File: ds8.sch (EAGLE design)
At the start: 79 parts, among them Q1 BC850, Q2 BC850, Q3 BC850, U1 LM13700M, U2 LM324, U3 LM324, U4 LM741D

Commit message: added some text infos
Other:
- note added: "Controls"
- note added: "Envelope"
- note added: "LFO"
- note added: "Noise"
- note added: "Output"
- note added: "Power Supply"
- note added: "VCA"
- note added: "VCO"
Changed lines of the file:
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@@
 <?xml version="1.0" encoding="utf-8"?>
 <!DOCTYPE eagle SYSTEM "eagle.dtd">
-<eagle version="6.1">
+<eagle version="6.3">
 <drawing>
 <settings>
@@
 <sheet>
 <plain>
+<text x="-25.4" y="-63.5" size="5.08" layer="91">Power Supply</text>
+<text x="7.62" y="48.26" size="5.08" layer="91">Envelope</text>
+<text x="167.64" y="30.48" size="5.08" layer="91">VCA</text>
+<text x="254" y="5.08" size="5.08" layer="91">Output</text>
+<text x="157.48" y="-111.76" size="5.08" layer="91">Noise</text>
+<text x="149.86" y="-40.64" size="5.08" layer="91">VCO</text>
+<text x="22.86" y="-25.4" size="5.08" layer="91">LFO</text>
+<text x="2.54" y="-121.92" size="5.08" layer="91">Controls</text>
 </plain>
 <instances>

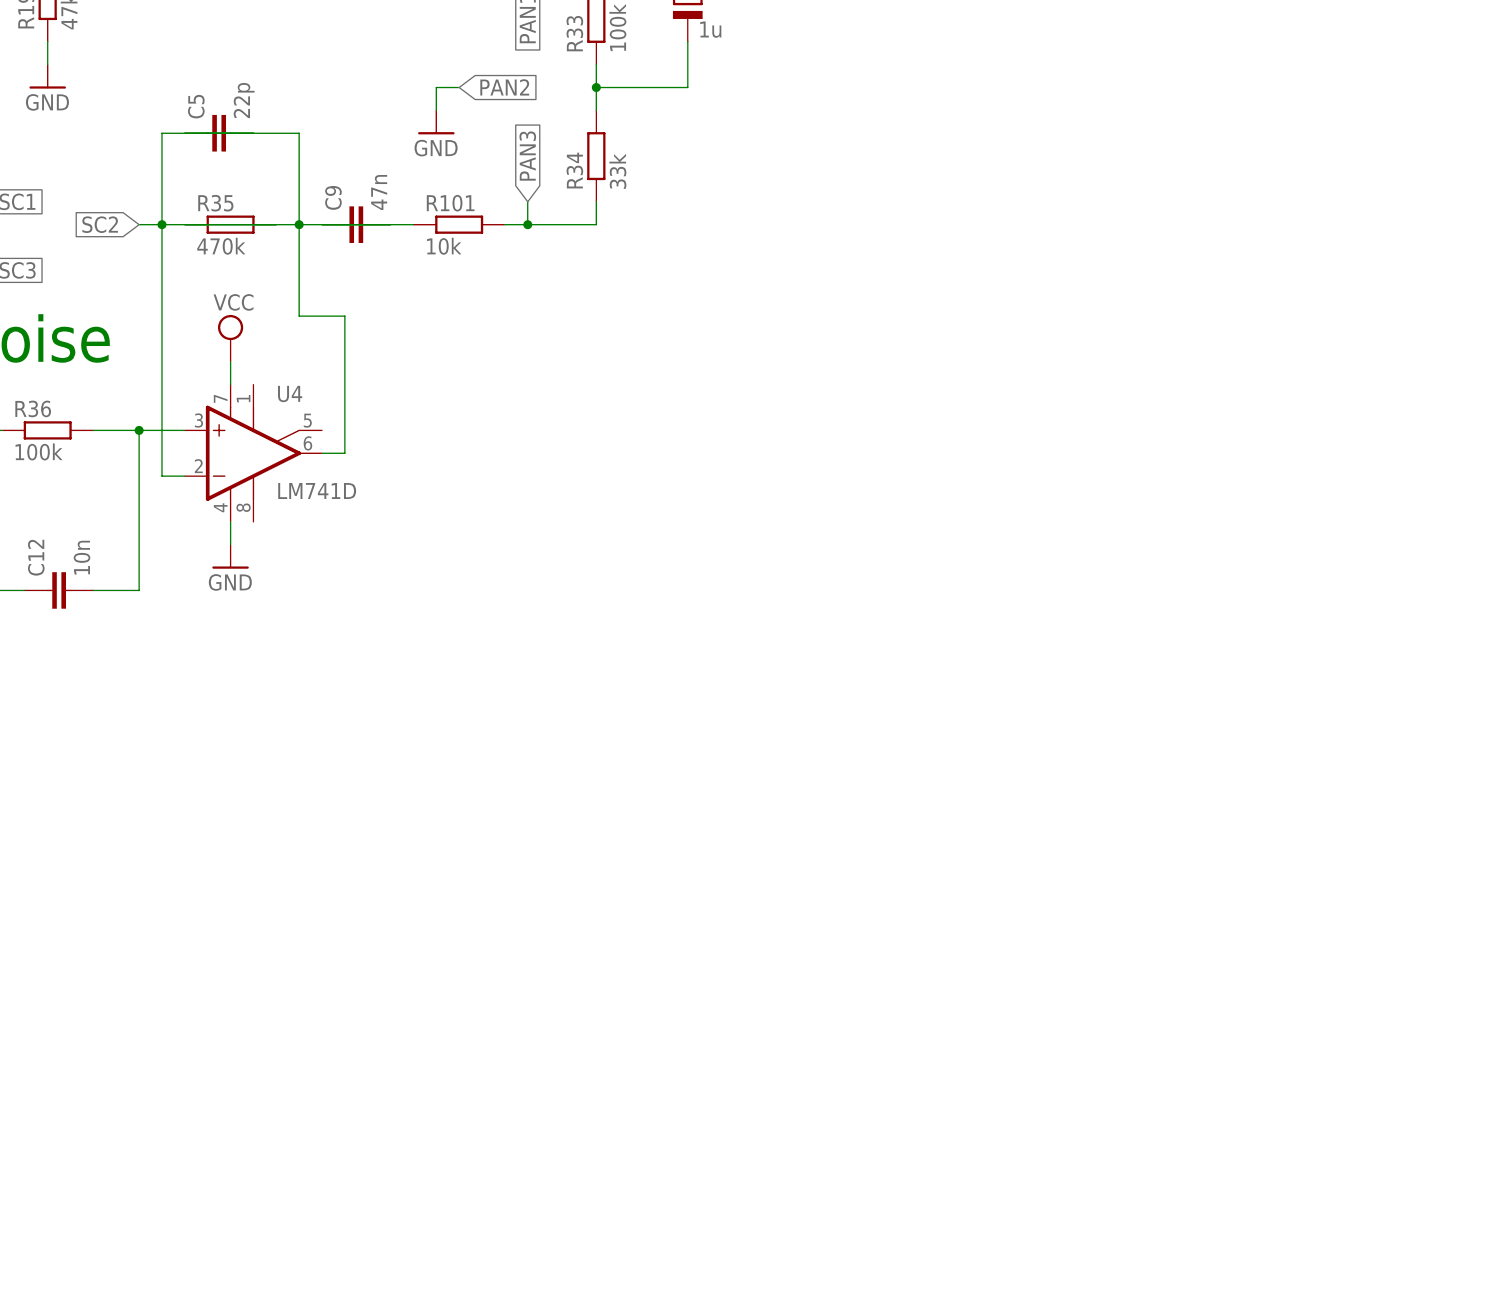
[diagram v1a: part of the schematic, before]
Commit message: added regulator for mcu
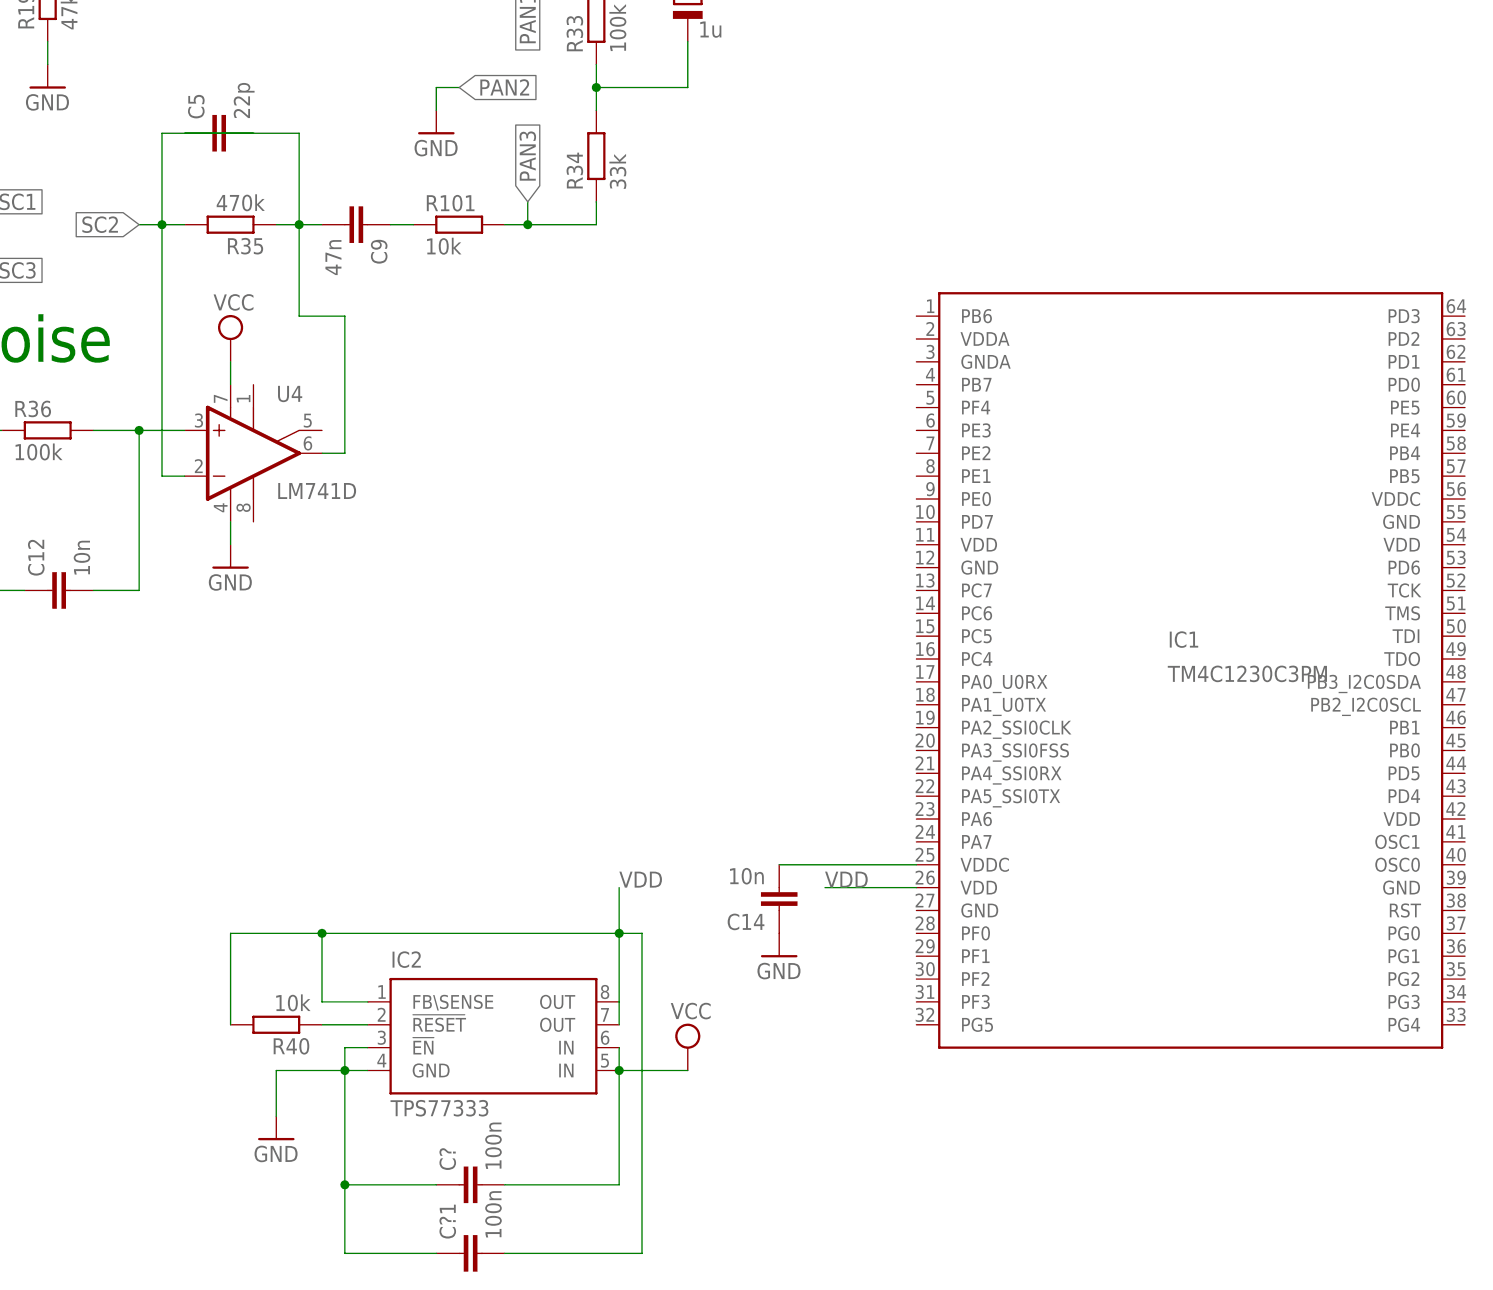
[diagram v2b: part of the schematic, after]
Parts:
- added C14: 10n, rcl:C-EUC1206
- added C?, C?1: 100n, rcl:C-EUC1206
- added IC1: TM4C1230C3PM, TM4:TM4C1230C3PM
- added IC2: TPS77333, texas:TPS77333
- added R40: 10k, rcl:R-EU_M0805
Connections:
- new net N$18: IC2.!RESET, R40.1
- new net N$6: C14.2, IC1.VDDC@0
- new net VDD: C?1.2, IC1.VDD@1, IC2.FB\SENSE, IC2.OUT@1, IC2.OUT@2, R40.2
- net GND: now also C14.1, C?.1, C?1.1, IC2.!EN, IC2.GND
- net VCC: now also C?.2, IC2.IN@1, IC2.IN@2
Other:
- moved on the sheet: C9, R35
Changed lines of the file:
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@@
 <part name="GND30" library="supply1" deviceset="GND" device=""/>
 <part name="GND31" library="supply1" deviceset="GND" device=""/>
+<part name="IC1" library="TM4" deviceset="TM4C1230C3PM" device=""/>
+<part name="IC2" library="texas" deviceset="TPS773*" device="" technology="33"/>
+<part name="SUPPLY10" library="supply2" deviceset="VCC" device=""/>
+<part name="GND32" library="supply1" deviceset="GND" device=""/>
+<part name="C?" library="rcl" deviceset="C-EU" device="C1206" value="100n"/>
+<part name="C?1" library="rcl" deviceset="C-EU" device="C1206" value="100n"/>
+<part name="R40" library="rcl" deviceset="R-EU_" device="M0805" value="10k"/>
+<part name="C14" library="rcl" deviceset="C-EU" device="C1206" value="10n"/>
+<part name="GND33" library="supply1" deviceset="GND" device=""/>
 </parts>
 <sheets>
@@
 <instance part="R33" gate="G$1" x="228.6" y="-73.66" rot="R90"/>
 <instance part="R34" gate="G$1" x="228.6" y="-88.9" rot="R90"/>
-<instance part="R35" gate="G$1" x="187.96" y="-96.52"/>
+<instance part="R35" gate="G$1" x="187.96" y="-96.52" rot="R180"/>
 <instance part="R36" gate="G$1" x="167.64" y="-119.38"/>
 <instance part="R37" gate="G$1" x="144.78" y="-129.54"/>
@@
 <instance part="SUPPLY6" gate="G$1" x="137.16" y="27.94"/>
 <instance part="GND15" gate="1" x="213.36" y="-43.18"/>
-<instance part="C9" gate="G$1" x="200.66" y="-96.52" rot="R90"/>
+<instance part="C9" gate="G$1" x="203.2" y="-96.52" rot="R270"/>
 <instance part="C10" gate="G$1" x="152.4" y="-93.98" rot="R90"/>
 <instance part="C11" gate="G$1" x="152.4" y="-101.6" rot="R90"/>
@@
 <instance part="GND30" gate="1" x="40.64" y="-172.72"/>
 <instance part="GND31" gate="1" x="68.58" y="-172.72"/>
+<instance part="IC1" gate="G$1" x="294.64" y="-144.78"/>
+<instance part="IC2" gate="G$1" x="215.9" y="-187.96"/>
+<instance part="SUPPLY10" gate="G$1" x="238.76" y="-187.96"/>
+<instance part="GND32" gate="1" x="193.04" y="-198.12"/>
+<instance part="C?" gate="G$1" x="213.36" y="-203.2" rot="R90"/>
+<instance part="C?1" gate="G$1" x="213.36" y="-210.82" rot="R90"/>
+<instance part="R40" gate="G$1" x="193.04" y="-185.42" rot="R180"/>
+<instance part="C14" gate="G$1" x="248.92" y="-172.72" rot="R180"/>
+<instance part="GND33" gate="1" x="248.92" y="-177.8"/>
 </instances>
 <busses>
@@
 <pinref part="GND29" gate="1" pin="GND"/>
 </segment>
+<segment>
+<pinref part="IC2" gate="G$1" pin="GND"/>
+<wire x1="203.2" y1="-190.5" x2="200.66" y2="-190.5" width="0.1524" layer="91"/>
+<pinref part="GND32" gate="1" pin="GND"/>
+<wire x1="200.66" y1="-190.5" x2="193.04" y2="-190.5" width="0.1524" layer="91"/>
+<wire x1="193.04" y1="-190.5" x2="193.04" y2="-195.58" width="0.1524" layer="91"/>
+<pinref part="IC2" gate="G$1" pin="!EN"/>
+<wire x1="203.2" y1="-187.96" x2="200.66" y2="-187.96" width="0.1524" layer="91"/>
+<wire x1="200.66" y1="-187.96" x2="200.66" y2="-190.5" width="0.1524" layer="91"/>
+<junction x="200.66" y="-190.5"/>
+<pinref part="C?" gate="G$1" pin="1"/>
+<wire x1="210.82" y1="-203.2" x2="200.66" y2="-203.2" width="0.1524" layer="91"/>
+<wire x1="200.66" y1="-203.2" x2="200.66" y2="-190.5" width="0.1524" layer="91"/>
+<wire x1="200.66" y1="-203.2" x2="200.66" y2="-210.82" width="0.1524" layer="91"/>
+<pinref part="C?1" gate="G$1" pin="1"/>
+<wire x1="200.66" y1="-210.82" x2="210.82" y2="-210.82" width="0.1524" layer="91"/>
+<junction x="200.66" y="-203.2"/>
+</segment>
+<segment>
+<pinref part="C14" gate="G$1" pin="1"/>
+<pinref part="GND33" gate="1" pin="GND"/>
+</segment>
 </net>
 <net name="VCC" class="0">
@@
 <wire x1="121.92" y1="-127" x2="121.92" y2="-129.54" width="0.1524" layer="91"/>
 <junction x="121.92" y="-129.54"/>
+</segment>
+<segment>
+<pinref part="IC2" gate="G$1" pin="IN@1"/>
+<pinref part="IC2" gate="G$1" pin="IN@2"/>
+<wire x1="231.14" y1="-190.5" x2="231.14" y2="-187.96" width="0.1524" layer="91"/>
+<pinref part="SUPPLY10" gate="G$1" pin="VCC"/>
+<wire x1="238.76" y1="-190.5" x2="231.14" y2="-190.5" width="0.1524" layer="91"/>
+<wire x1="231.14" y1="-190.5" x2="231.14" y2="-203.2" width="0.1524" layer="91"/>
+<pinref part="C?" gate="G$1" pin="2"/>
+<wire x1="231.14" y1="-203.2" x2="218.44" y2="-203.2" width="0.1524" layer="91"/>
+<junction x="231.14" y="-190.5"/>
 </segment>
 </net>
@@
 <pinref part="R101" gate="G$1" pin="1"/>
 <pinref part="C9" gate="G$1" pin="1"/>
-<wire x1="208.28" y1="-96.52" x2="198.12" y2="-96.52" width="0.1524" layer="91"/>
+<wire x1="208.28" y1="-96.52" x2="205.74" y2="-96.52" width="0.1524" layer="91"/>
 </segment>
 </net>
@@
 <pinref part="C9" gate="G$1" pin="2"/>
 <pinref part="R35" gate="G$1" pin="1"/>
-<wire x1="205.74" y1="-96.52" x2="195.58" y2="-96.52" width="0.1524" layer="91"/>
+<wire x1="198.12" y1="-96.52" x2="195.58" y2="-96.52" width="0.1524" layer="91"/>
 <pinref part="C5" gate="G$1" pin="1"/>
-<wire x1="195.58" y1="-96.52" x2="182.88" y2="-96.52" width="0.1524" layer="91"/>
+<wire x1="195.58" y1="-96.52" x2="193.04" y2="-96.52" width="0.1524" layer="91"/>
 <wire x1="182.88" y1="-86.36" x2="195.58" y2="-86.36" width="0.1524" layer="91"/>
 <wire x1="195.58" y1="-86.36" x2="195.58" y2="-96.52" width="0.1524" layer="91"/>
@@
 <segment>
 <pinref part="R35" gate="G$1" pin="2"/>
-<wire x1="193.04" y1="-96.52" x2="180.34" y2="-96.52" width="0.1524" layer="91"/>
+<wire x1="182.88" y1="-96.52" x2="180.34" y2="-96.52" width="0.1524" layer="91"/>
 <wire x1="180.34" y1="-96.52" x2="180.34" y2="-86.36" width="0.1524" layer="91"/>
 <pinref part="C5" gate="G$1" pin="2"/>
@@
 </segment>
 </net>
+<net name="VDD" class="0">
+<segment>
+<pinref part="IC2" gate="G$1" pin="OUT@1"/>
+<pinref part="IC2" gate="G$1" pin="OUT@2"/>
+<wire x1="231.14" y1="-185.42" x2="231.14" y2="-182.88" width="0.1524" layer="91"/>
+<wire x1="231.14" y1="-182.88" x2="231.14" y2="-175.26" width="0.1524" layer="91"/>
+<label x="231.14" y="-170.18" size="1.778" layer="95"/>
+<pinref part="IC2" gate="G$1" pin="FB\SENSE"/>
+<wire x1="231.14" y1="-175.26" x2="231.14" y2="-170.18" width="0.1524" layer="91"/>
+<wire x1="203.2" y1="-182.88" x2="198.12" y2="-182.88" width="0.1524" layer="91"/>
+<wire x1="198.12" y1="-182.88" x2="198.12" y2="-175.26" width="0.1524" layer="91"/>
+<wire x1="198.12" y1="-175.26" x2="231.14" y2="-175.26" width="0.1524" layer="91"/>
+<junction x="231.14" y="-175.26"/>
+<pinref part="C?1" gate="G$1" pin="2"/>
+<wire x1="218.44" y1="-210.82" x2="233.68" y2="-210.82" width="0.1524" layer="91"/>
+<wire x1="233.68" y1="-210.82" x2="233.68" y2="-175.26" width="0.1524" layer="91"/>
+<wire x1="233.68" y1="-175.26" x2="231.14" y2="-175.26" width="0.1524" layer="91"/>
+<pinref part="R40" gate="G$1" pin="2"/>
+<wire x1="187.96" y1="-185.42" x2="187.96" y2="-175.26" width="0.1524" layer="91"/>
+<wire x1="187.96" y1="-175.26" x2="198.12" y2="-175.26" width="0.1524" layer="91"/>
+<junction x="198.12" y="-175.26"/>
+</segment>
+<segment>
+<pinref part="IC1" gate="G$1" pin="VDD@1"/>
+<label x="254" y="-170.18" size="1.778" layer="95"/>
+<wire x1="254" y1="-170.18" x2="264.16" y2="-170.18" width="0.1524" layer="91"/>
+</segment>
+</net>
+<net name="N$18" class="0">
+<segment>
+<pinref part="IC2" gate="G$1" pin="!RESET"/>
+<pinref part="R40" gate="G$1" pin="1"/>
+<wire x1="203.2" y1="-185.42" x2="198.12" y2="-185.42" width="0.1524" layer="91"/>
+</segment>
+</net>
+<net name="N$6" class="0">
+<segment>
+<pinref part="IC1" gate="G$1" pin="VDDC@0"/>
+<pinref part="C14" gate="G$1" pin="2"/>
+<wire x1="264.16" y1="-167.64" x2="248.92" y2="-167.64" width="0.1524" layer="91"/>
+</segment>
+</net>
